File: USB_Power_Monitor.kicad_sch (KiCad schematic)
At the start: 53 parts, among them IC1 MCS1826GQTE-05-P, J1 USB_C_Receptacle, J2 USB_C_Plug, J3 OLED, SW1 SW_Push_Dual, U1 RP2040, U2 L7983PU33R, U3 W25Q16JVSS, U4 TS3USB221AQRSERQ1, Y1 ABM8-272-T3

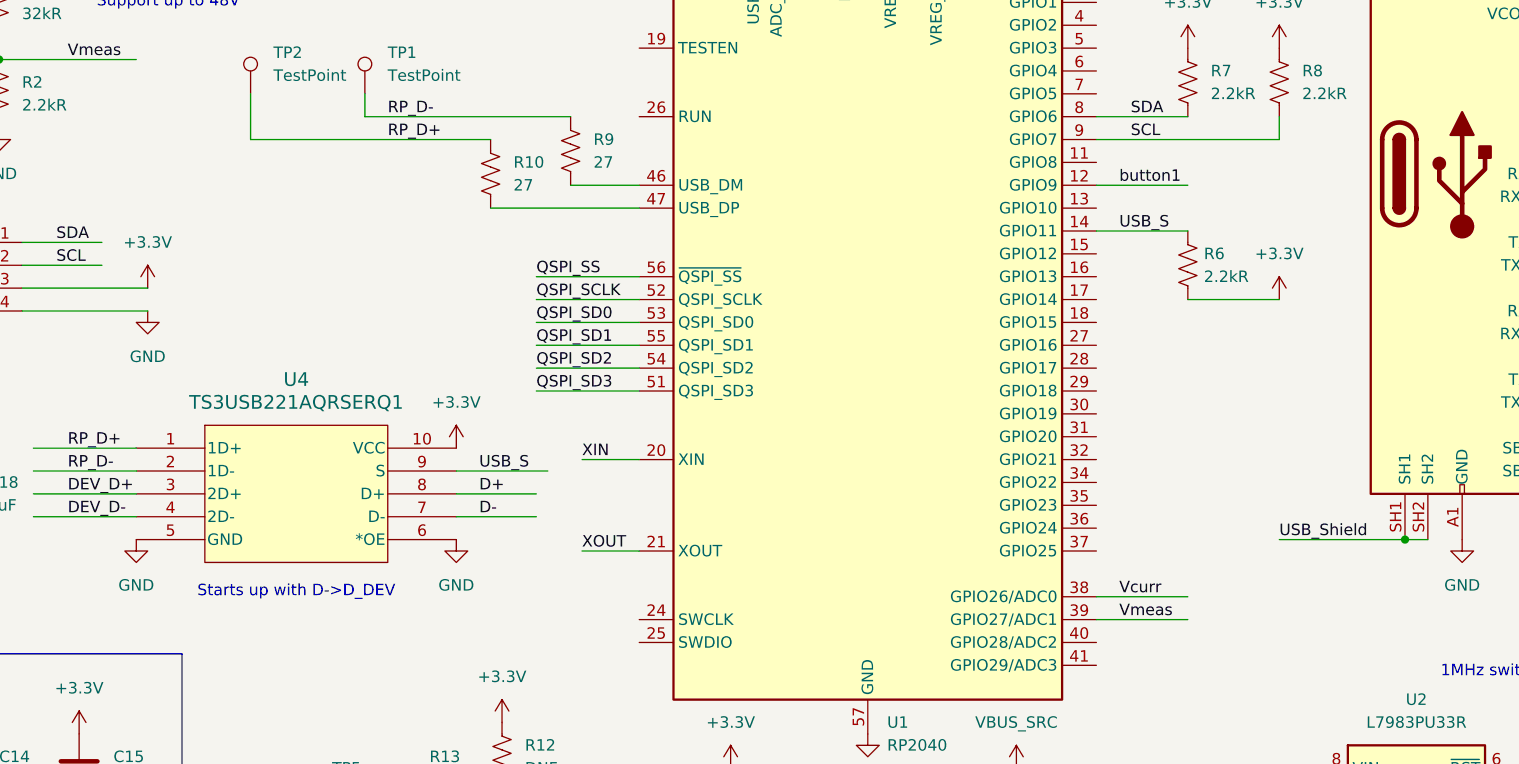
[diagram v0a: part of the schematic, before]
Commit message: finished routing RP2040
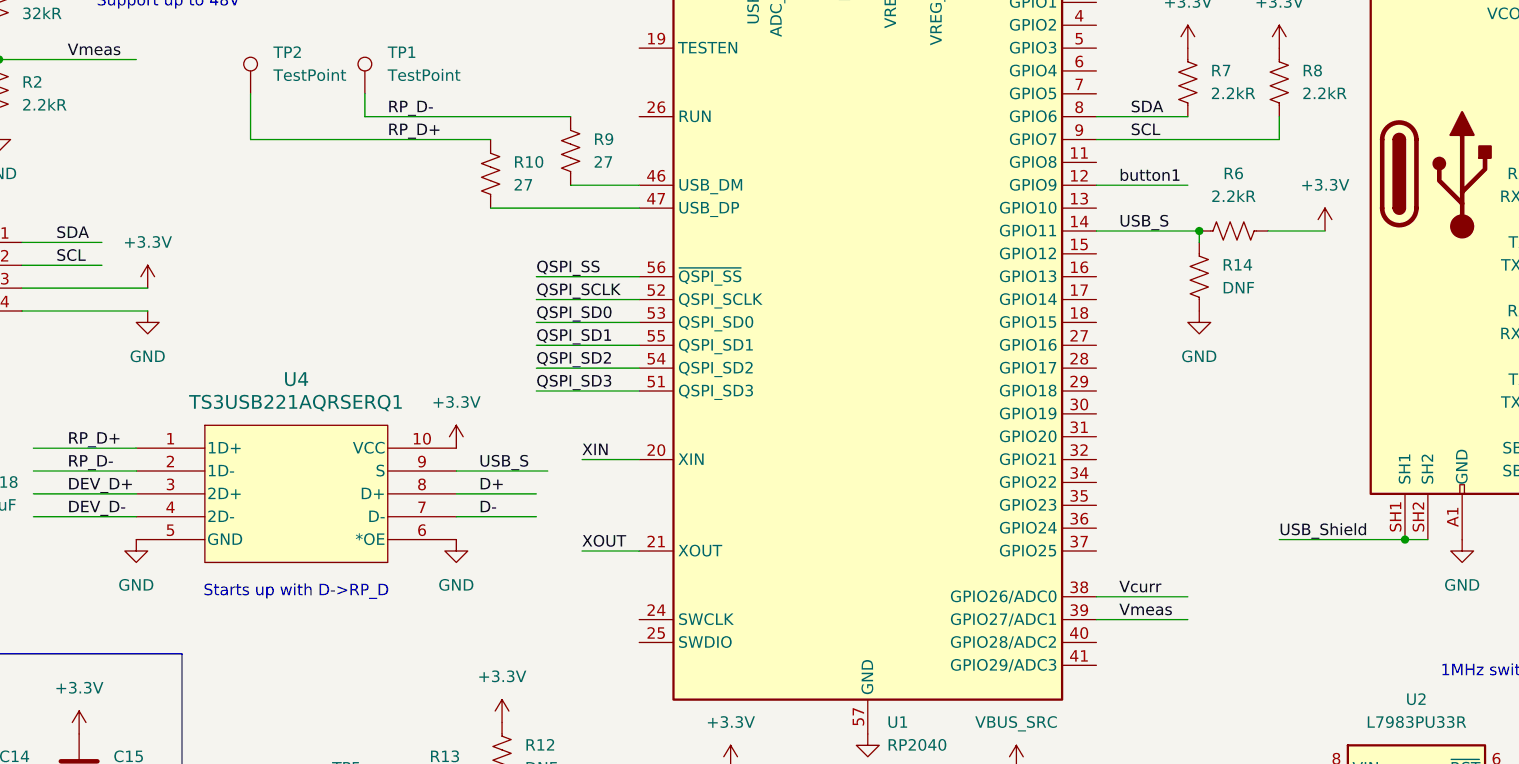
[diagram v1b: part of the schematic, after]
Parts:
- added R14: DNF, Capacitor_SMD:C_0603_1608Metric, symbol Device:R_US
- C20, C21: footprint (none) -> Capacitor_SMD:C_0603_1608Metric; Manufacturer_Name (none) -> YAGEO; Manufacturer_Part_Number (none) -> CC0603JRNPO9BN150
- R10, R9: footprint (none) -> Capacitor_SMD:C_0603_1608Metric; Manufacturer_Name (none) -> YAGEO; Manufacturer_Part_Number (none) -> RC0603FR-0727RL
- R11, R13: footprint (none) -> Capacitor_SMD:C_0603_1608Metric; Manufacturer_Name (none) -> YAGEO; Manufacturer_Part_Number (none) -> RC0603FR-071KL
- R12: footprint (none) -> Capacitor_SMD:C_0603_1608Metric
- TP1, TP2, TP3, TP4: footprint TestPoint:TestPoint_Pad_D2.0mm -> TestPoint:TestPoint_Pad_1.0x1.0mm
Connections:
- net GND: now also R14.1
- net USB_S: now also R14.2
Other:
- note added: "Starts up with D->RP_D"
- note removed: "Starts up with D->D_DEV"
- moved on the sheet: R6

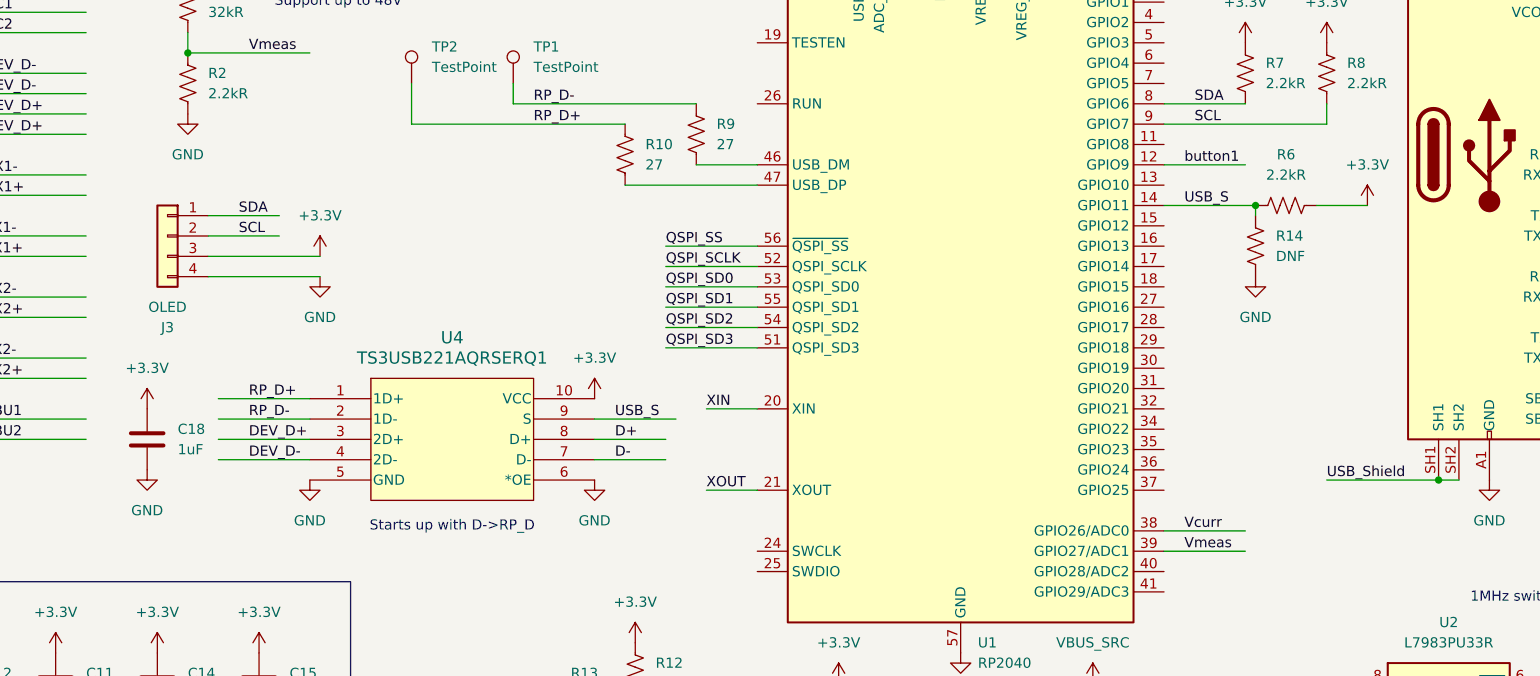
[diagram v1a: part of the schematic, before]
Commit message: finished routing most components, no power yet
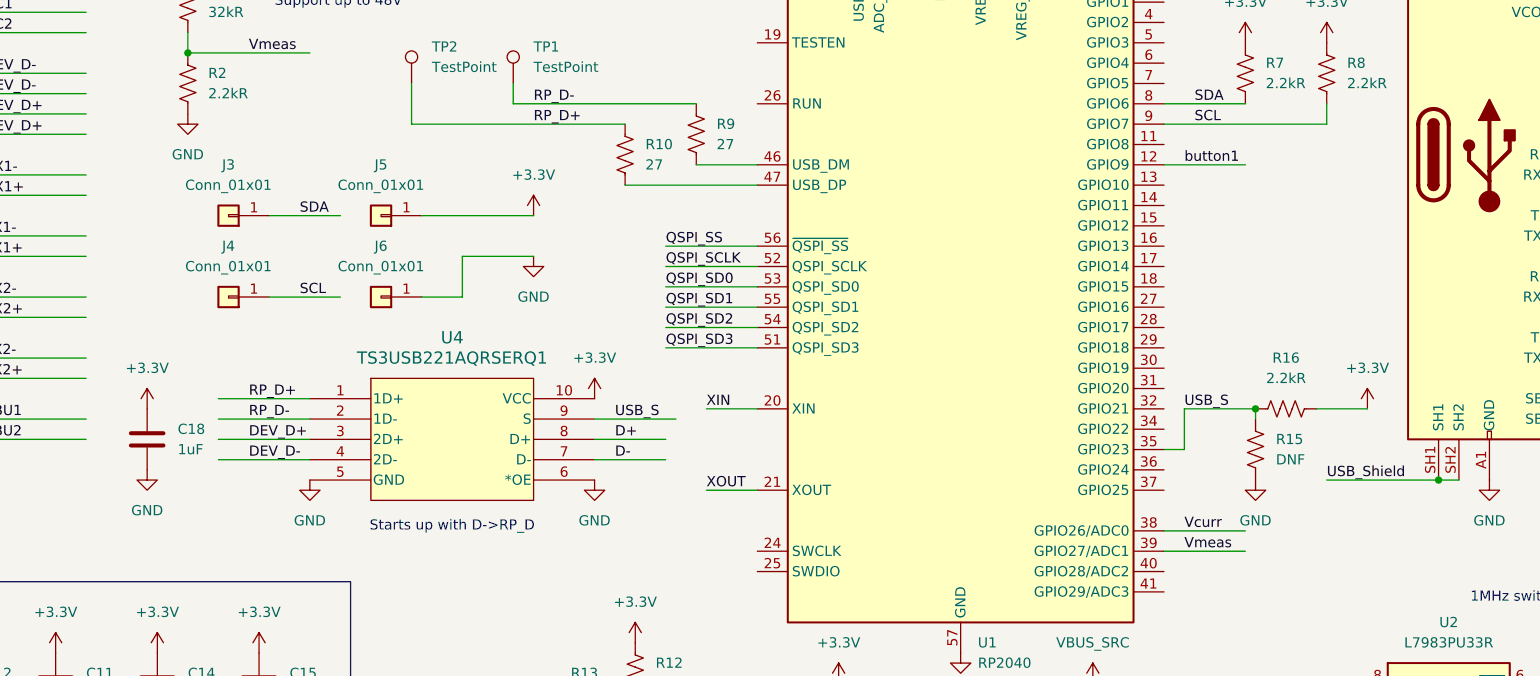
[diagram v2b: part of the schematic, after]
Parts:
- removed J3: OLED, Connector_PinHeader_2.54mm:PinHeader_1x04_P2.54mm_Vertical, symbol Connector_Generic:Conn_01x04
- removed R14: DNF, Capacitor_SMD:C_0603_1608Metric, symbol Device:R_US
- removed R6: 2.2kR, Capacitor_SMD:C_0603_1608Metric, symbol Device:R_US
- added J3, J4, J5, J6: Conn_01x01, Connector_PinHeader_2.54mm:PinHeader_1x01_P2.54mm_Vertical, symbol Connector_Generic:Conn_01x01
- added R15: DNF, Capacitor_SMD:C_0603_1608Metric, symbol Device:R_US
- added R16: 2.2kR, Capacitor_SMD:C_0603_1608Metric, symbol Device:R_US
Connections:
- net +3.3V: now also J5.1 (Pin_1), R16.2
- net GND: now also J6.1 (Pin_1), R15.1
- net SCL: now also J4.1 (Pin_1)
- net SDA: now also J3.1 (Pin_1)
- net USB_S: now also U1.35 (GPIO23), R15.2, R16.1; no longer U1.14 (GPIO11)

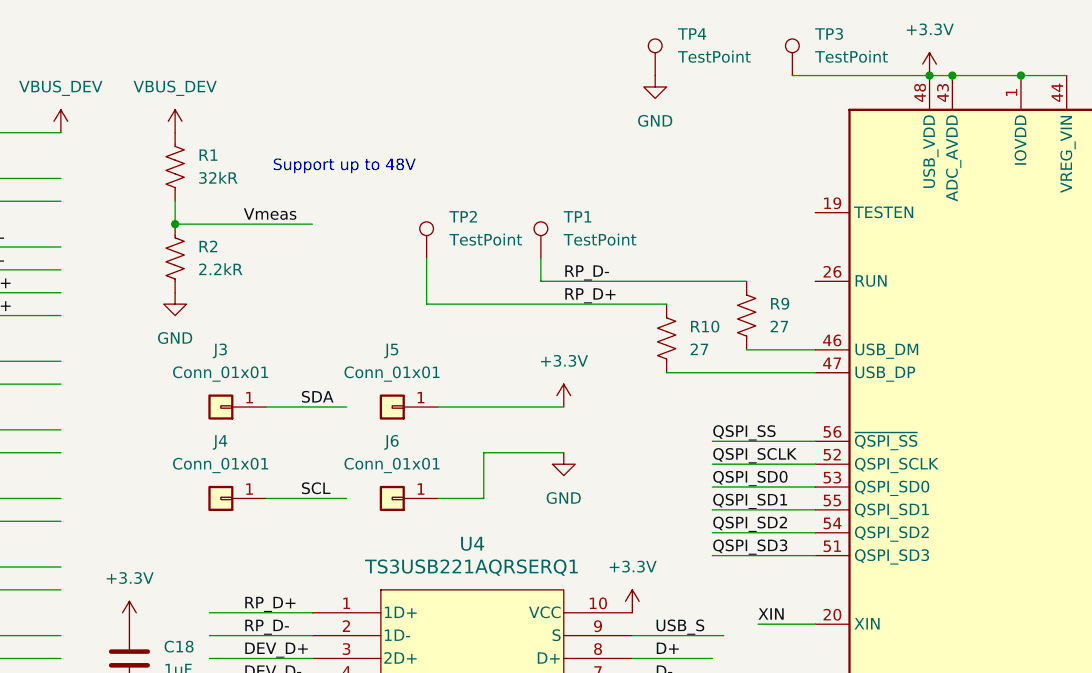
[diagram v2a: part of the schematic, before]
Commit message: Main power zone defined
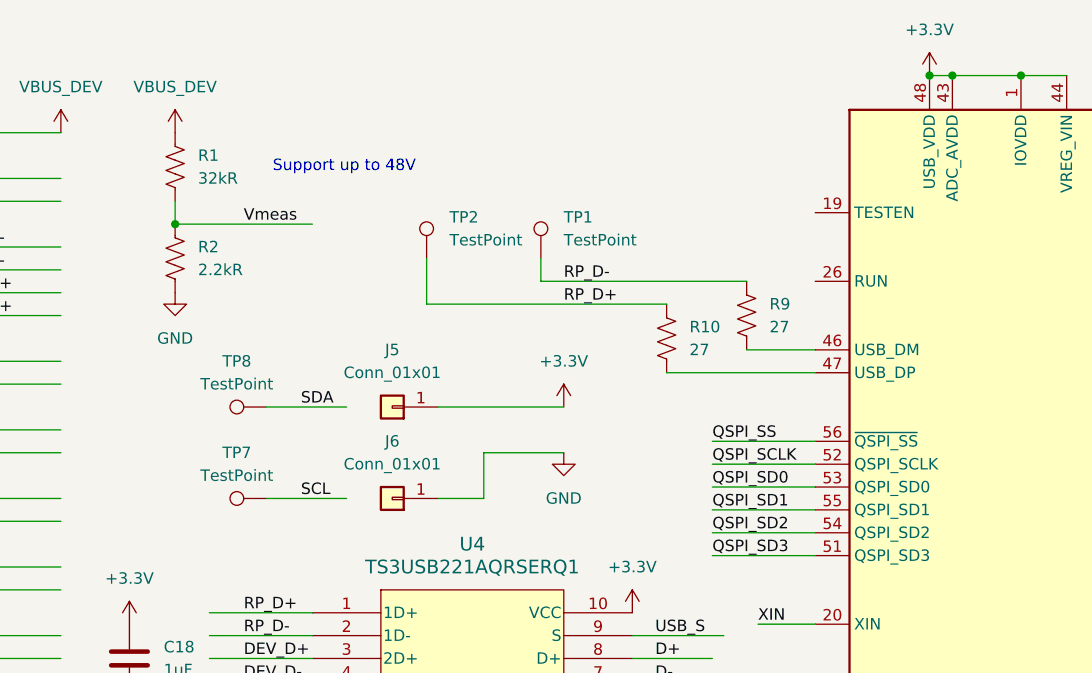
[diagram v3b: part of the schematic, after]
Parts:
- removed J3, J4: Conn_01x01, Connector_PinHeader_2.54mm:PinHeader_1x01_P2.54mm_Vertical, symbol Connector_Generic:Conn_01x01
- removed TP3, TP4: TestPoint, TestPoint:TestPoint_Pad_1.0x1.0mm, symbol Connector:TestPoint
- added TP7, TP8: TestPoint, TestPoint:TestPoint_Pad_1.0x1.0mm, symbol Connector:TestPoint
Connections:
- net SCL: now also TP7.1
- net SDA: now also TP8.1
